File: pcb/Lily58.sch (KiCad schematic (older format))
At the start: 114 parts, among them J1 LED, J2 4PIN, J3 Conn_01x06_Female, P1 i2c_pin, P2 i2c_pin, SW1 SW_PUSH, SW10 SW_PUSH, SW11 SW_PUSH, SW12 SW_PUSH, SW13 SW_PUSH, SW14 SW_PUSH, SW15 SW_PUSH, SW16 SW_PUSH, SW17 SW_PUSH, SW18 SW_PUSH, SW19 SW_PUSH, SW2 SW_PUSH, SW20 SW_PUSH, SW21 SW_PUSH, SW22 SW_PUSH, SW23 SW_PUSH, SW24 SW_PUSH, SW25 SW_PUSH, SW26 SW_PUSH, SW27 SW_PUSH, SW28 SW_PUSH, SW29 SW_PUSH, SW3 SW_PUSH, SW4 SW_PUSH, SW5 SW_PUSH, SW6 SW_PUSH, SW7 SW_PUSH, SW8 SW_PUSH, SW9 SW_PUSH, U1 ProMicro

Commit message: add pinheader and logo
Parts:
- added J4: Conn_01x06_Female, Lily58-footprint:OLED_4Pin, symbol Lily58-rescue:CONN_01X04-Lily58-cache
- added JP10, JP11, JP12, JP13, JP14, JP15, JP16, JP9: Jumper_NO_Small, Lily58-footprint:Jumper, symbol Device:Jumper_NO_Small
- J3: symbol Connector:Conn_01x06_Female -> Lily58-rescue:CONN_01X04-Lily58-cache
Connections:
- net A2: now also JP11.2, JP14.2; no longer J3.6 (Pin_6)
- net A3: now also JP12.2, JP13.2; no longer J3.5 (Pin_5)
- net col0: now also JP10.2, JP15.2
- net row4: now also JP16.2, JP9.2
- new net: J4.1 (P1), JP13.1, JP9.1
- new net: J4.2 (P2), JP10.1, JP14.1
- new net: J4.3 (P3), JP11.1, JP15.1
- new net: J4.4 (P4), JP12.1, JP16.1
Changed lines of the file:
@@
 $EndComp
 $Comp
-L Connector:Conn_01x06_Female J3
+L Lily58-rescue:CONN_01X04-Lily58-cache J3
 U 1 1 6192B632
-P 2550 6250
-F 0 "J3" H 2578 6226 50  0000 L CNN
-F 1 "Conn_01x06_Female" H 2578 6135 50  0000 L CNN
-F 2 "Lily58-footprint:OLED_4Pin" H 2550 6250 50  0001 C CNN
-F 3 "~" H 2550 6250 50  0001 C CNN
-	1    2550 6250
-	1    0    0    -1
+P 2150 6200
+F 0 "J3" H 2178 6176 50  0000 L CNN
+F 1 "Conn_01x06_Female" H 2178 6085 50  0000 L CNN
+F 2 "Lily58-footprint:OLED_4Pin" H 2150 6200 50  0001 C CNN
+F 3 "~" H 2150 6200 50  0001 C CNN
+	1    2150 6200
+	-1   0    0    -1
 $EndComp
 Wire Wire Line
@@
 Text GLabel 4050 2600 2    50   Input ~ 0
 A2
-Text GLabel 2350 6450 0    50   Input ~ 0
-A3
-Text GLabel 2350 6550 0    50   Input ~ 0
-A2
 Text GLabel 5500 7050 0    50   Input ~ 0
 LED
+$Comp
+L Lily58-rescue:CONN_01X04-Lily58-cache J4
+U 1 1 6197A369
+P 2150 7150
+F 0 "J4" H 2178 7126 50  0000 L CNN
+F 1 "Conn_01x06_Female" H 2178 7035 50  0000 L CNN
+F 2 "Lily58-footprint:OLED_4Pin" H 2150 7150 50  0001 C CNN
+F 3 "~" H 2150 7150 50  0001 C CNN
+	1    2150 7150
+	-1   0    0    -1
+$EndComp
+Text GLabel 3050 7300 2    50   Input ~ 0
+A3
+Text GLabel 3050 7200 2    50   Input ~ 0
+A2
+Text GLabel 3050 7100 2    50   Input ~ 0
+col0
+Text GLabel 3050 7000 2    50   Input ~ 0
+row4
+Text GLabel 3050 7500 2    50   Input ~ 0
+A3
+Text GLabel 3050 7600 2    50   Input ~ 0
+A2
+Text GLabel 3050 7700 2    50   Input ~ 0
+col0
+Text GLabel 3050 7800 2    50   Input ~ 0
+row4
+$Comp
+L Device:Jumper_NO_Small JP9
+U 1 1 619CD29F
+P 2950 7000
+F 0 "JP9" H 2950 6950 50  0000 C CNN
+F 1 "Jumper_NO_Small" H 2950 7094 50  0001 C CNN
+F 2 "Lily58-footprint:Jumper" H 2950 7000 50  0001 C CNN
+F 3 "~" H 2950 7000 50  0001 C CNN
+	1    2950 7000
+	1    0    0    -1
+$EndComp
+$Comp
+L Device:Jumper_NO_Small JP10
+U 1 1 619CDE91
+P 2950 7100
+F 0 "JP10" H 2950 7050 50  0000 C CNN
+F 1 "Jumper_NO_Small" H 2950 7194 50  0001 C CNN
+F 2 "Lily58-footprint:Jumper" H 2950 7100 50  0001 C CNN
+F 3 "~" H 2950 7100 50  0001 C CNN
+	1    2950 7100
+	1    0    0    -1
+$EndComp
+$Comp
+L Device:Jumper_NO_Small JP11
+U 1 1 619CDE9B
+P 2950 7200
+F 0 "JP11" H 2950 7150 50  0000 C CNN
+F 1 "Jumper_NO_Small" H 2950 7294 50  0001 C CNN
+F 2 "Lily58-footprint:Jumper" H 2950 7200 50  0001 C CNN
+F 3 "~" H 2950 7200 50  0001 C CNN
+	1    2950 7200
+	1    0    0    -1
+$EndComp
+$Comp
+L Device:Jumper_NO_Small JP12
+U 1 1 619CDEA5
+P 2950 7300
+F 0 "JP12" H 2950 7250 50  0000 C CNN
+F 1 "Jumper_NO_Small" H 2950 7394 50  0001 C CNN
+F 2 "Lily58-footprint:Jumper" H 2950 7300 50  0001 C CNN
+F 3 "~" H 2950 7300 50  0001 C CNN
+	1    2950 7300
+	1    0    0    -1
+$EndComp
+$Comp
+L Device:Jumper_NO_Small JP13
+U 1 1 619CDEAF
+P 2950 7500
+F 0 "JP13" H 2950 7450 50  0000 C CNN
+F 1 "Jumper_NO_Small" H 2950 7594 50  0001 C CNN
+F 2 "Lily58-footprint:Jumper" H 2950 7500 50  0001 C CNN
+F 3 "~" H 2950 7500 50  0001 C CNN
+	1    2950 7500
+	1    0    0    -1
+$EndComp
+$Comp
+L Device:Jumper_NO_Small JP14
+U 1 1 619CDEB9
+P 2950 7600
+F 0 "JP14" H 2950 7550 50  0000 C CNN
+F 1 "Jumper_NO_Small" H 2950 7694 50  0001 C CNN
+F 2 "Lily58-footprint:Jumper" H 2950 7600 50  0001 C CNN
+F 3 "~" H 2950 7600 50  0001 C CNN
+	1    2950 7600
+	1    0    0    -1
+$EndComp
+$Comp
+L Device:Jumper_NO_Small JP15
+U 1 1 619CDEC3
+P 2950 7700
+F 0 "JP15" H 2950 7650 50  0000 C CNN
+F 1 "Jumper_NO_Small" H 2950 7794 50  0001 C CNN
+F 2 "Lily58-footprint:Jumper" H 2950 7700 50  0001 C CNN
+F 3 "~" H 2950 7700 50  0001 C CNN
+	1    2950 7700
+	1    0    0    -1
+$EndComp
+$Comp
+L Device:Jumper_NO_Small JP16
+U 1 1 619CDECD
+P 2950 7800
+F 0 "JP16" H 2950 7750 50  0000 C CNN
+F 1 "Jumper_NO_Small" H 2950 7894 50  0001 C CNN
+F 2 "Lily58-footprint:Jumper" H 2950 7800 50  0001 C CNN
+F 3 "~" H 2950 7800 50  0001 C CNN
+	1    2950 7800
+	1    0    0    -1
+$EndComp
+Wire Wire Line
+	2350 7000 2800 7000
+Wire Wire Line
+	2350 7100 2750 7100
+Wire Wire Line
+	2350 7200 2700 7200
+Wire Wire Line
+	2350 7300 2650 7300
+Wire Wire Line
+	2800 7000 2800 7500
+Wire Wire Line
+	2800 7500 2850 7500
+Connection ~ 2800 7000
+Wire Wire Line
+	2800 7000 2850 7000
+Wire Wire Line
+	2850 7600 2750 7600
+Wire Wire Line
+	2750 7600 2750 7100
+Connection ~ 2750 7100
+Wire Wire Line
+	2750 7100 2850 7100
+Wire Wire Line
+	2850 7700 2700 7700
+Wire Wire Line
+	2700 7700 2700 7200
+Connection ~ 2700 7200
+Wire Wire Line
+	2700 7200 2850 7200
+Wire Wire Line
+	2850 7800 2650 7800
+Wire Wire Line
+	2650 7800 2650 7300
+Connection ~ 2650 7300
+Wire Wire Line
+	2650 7300 2850 7300
 $EndSCHEMATC

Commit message: brush up PCB
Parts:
- removed J1: LED, Lily58-footprint:StripLED, symbol Lily58-rescue:LED-Lily58-cache
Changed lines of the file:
@@
 $EndComp
-$Comp
-L Lily58-rescue:LED-Lily58-cache J1
-U 1 1 5B74AE32
-P 4000 3600
-F 0 "J1" H 4000 3800 50  0000 C CNN
-F 1 "LED" H 4000 3400 50  0000 C CNN
-F 2 "Lily58-footprint:StripLED" H 4000 3600 50  0001 C CNN
-F 3 "" H 4000 3600 50  0001 C CNN
-	1    4000 3600
-	1    0    0    -1
-$EndComp
-$Comp
-L Lily58-rescue:VCC-Lily58-cache #PWR07
-U 1 1 5B74B06A
-P 4200 3500
-F 0 "#PWR07" H 4200 3350 50  0001 C CNN
-F 1 "VCC" H 4217 3673 50  0000 C CNN
-F 2 "" H 4200 3500 50  0001 C CNN
-F 3 "" H 4200 3500 50  0001 C CNN
-	1    4200 3500
-	1    0    0    -1
-$EndComp
-$Comp
-L Lily58-rescue:GND-Lily58-cache #PWR08
-U 1 1 5B74B15A
-P 4200 3700
-F 0 "#PWR08" H 4200 3450 50  0001 C CNN
-F 1 "GND" H 4205 3527 50  0000 C CNN
-F 2 "" H 4200 3700 50  0001 C CNN
-F 3 "" H 4200 3700 50  0001 C CNN
-	1    4200 3700
-	1    0    0    -1
-$EndComp
-Text GLabel 4200 3600 2    50   Input ~ 0
-LED
 $Comp
 L Lily58-rescue:GND-Lily58-cache #PWR010

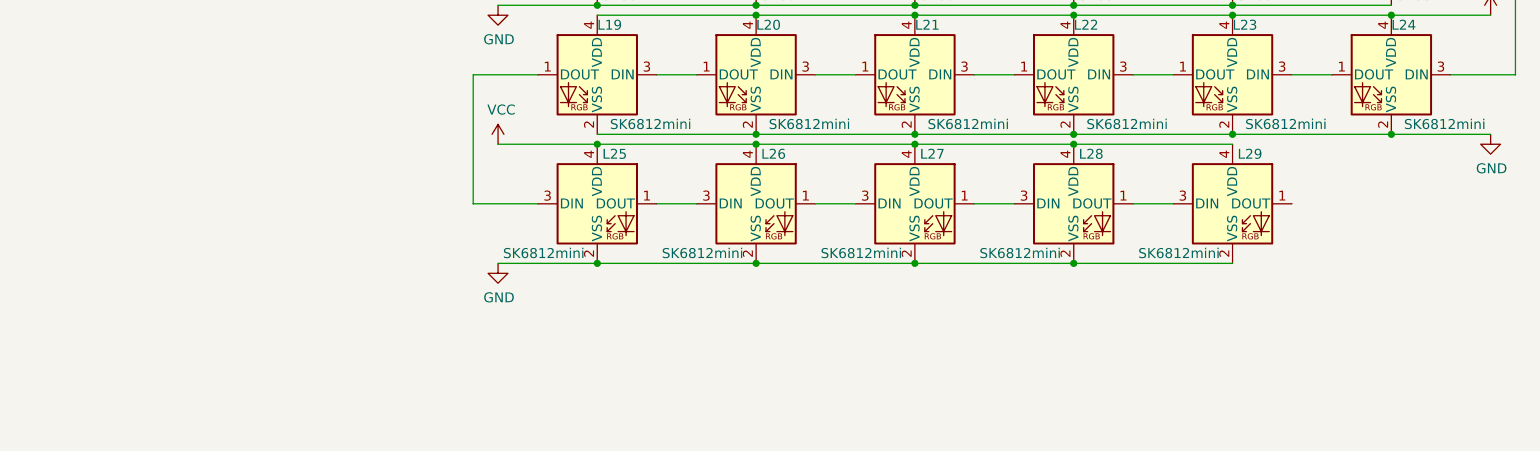
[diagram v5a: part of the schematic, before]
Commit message: add sk6812mini
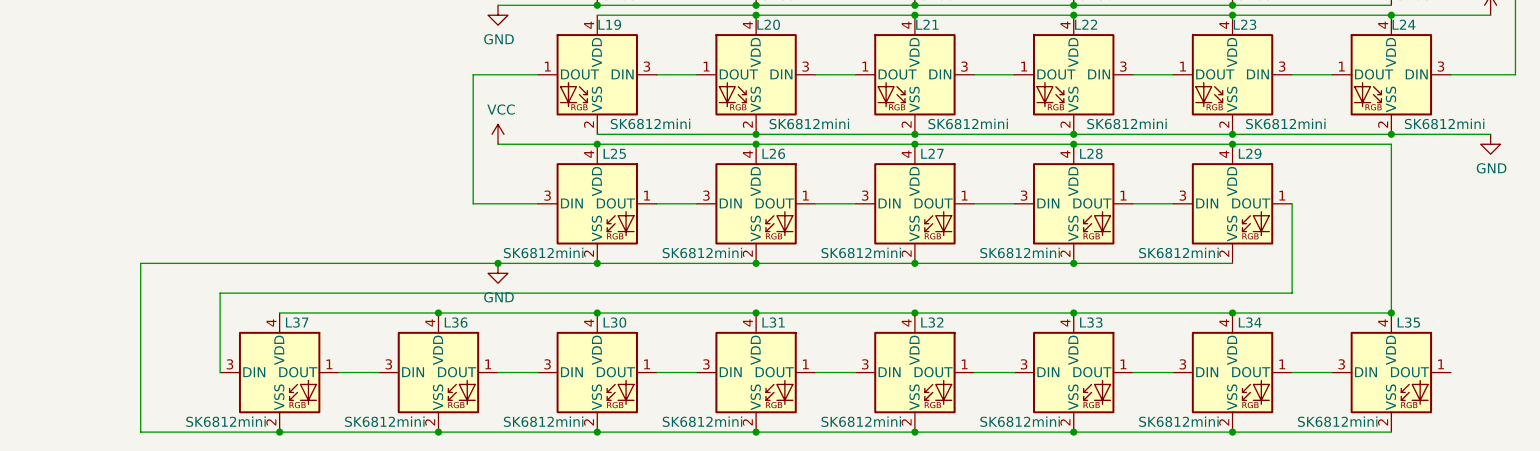
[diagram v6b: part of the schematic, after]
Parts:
- added L30, L31, L32, L33, L34, L35, L36, L37: SK6812mini, Lily58-footprint:SK6812MINI_underglow_rev, symbol LED:SK6812MINI
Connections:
- net GND: now also L30.2 (VSS), L31.2 (VSS), L32.2 (VSS), L33.2 (VSS), L34.2 (VSS), L35.2 (VSS), L36.2 (VSS), L37.2 (VSS)
- net VCC: now also L30.4 (VDD), L31.4 (VDD), L32.4 (VDD), L33.4 (VDD), L34.4 (VDD), L35.4 (VDD), L36.4 (VDD), L37.4 (VDD)
- net at L29.1 (DOUT): now also L37.3 (DIN)
- new net: L33.1 (DOUT), L34.3 (DIN)
- new net: L32.1 (DOUT), L33.3 (DIN)
- new net: L31.1 (DOUT), L32.3 (DIN)
- new net: L30.1 (DOUT), L31.3 (DIN)
- new net: L30.3 (DIN), L36.1 (DOUT)
- new net: L34.1 (DOUT), L35.3 (DIN)
- new net: L36.3 (DIN), L37.1 (DOUT)
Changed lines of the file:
@@
 	5500 7700 5175 7700
 Connection ~ 5800 9950
-Wire Wire Line
-	5300 9950 5800 9950
 Connection ~ 5800 8650
 Wire Wire Line
@@
 Wire Wire Line
 	2650 7300 2850 7300
+Wire Wire Line
+	7700 10500 7900 10500
+Wire Wire Line
+	6900 10500 7100 10500
+$Comp
+L LED:SK6812MINI L33
+U 1 1 61A4CA14
+P 8200 10500
+F 0 "L33" H 8225 10750 50  0000 L CNN
+F 1 "SK6812mini" H 7725 10250 50  0000 L CNN
+F 2 "Lily58-footprint:SK6812MINI_underglow_rev" H 8250 10200 50  0001 L TNN
+F 3 "https://cdn-shop.adafruit.com/product-files/2686/SK6812MINI_REV.01-1-2.pdf" H 8300 10125 50  0001 L TNN
+	1    8200 10500
+	1    0    0    -1
+$EndComp
+$Comp
+L LED:SK6812MINI L32
+U 1 1 61A4CA1E
+P 7400 10500
+F 0 "L32" H 7425 10750 50  0000 L CNN
+F 1 "SK6812mini" H 6925 10250 50  0000 L CNN
+F 2 "Lily58-footprint:SK6812MINI_underglow_rev" H 7450 10200 50  0001 L TNN
+F 3 "https://cdn-shop.adafruit.com/product-files/2686/SK6812MINI_REV.01-1-2.pdf" H 7500 10125 50  0001 L TNN
+	1    7400 10500
+	1    0    0    -1
+$EndComp
+Wire Wire Line
+	6100 10500 6300 10500
+$Comp
+L LED:SK6812MINI L31
+U 1 1 61A4CA29
+P 6600 10500
+F 0 "L31" H 6625 10750 50  0000 L CNN
+F 1 "SK6812mini" H 6125 10250 50  0000 L CNN
+F 2 "Lily58-footprint:SK6812MINI_underglow_rev" H 6650 10200 50  0001 L TNN
+F 3 "https://cdn-shop.adafruit.com/product-files/2686/SK6812MINI_REV.01-1-2.pdf" H 6700 10125 50  0001 L TNN
+	1    6600 10500
+	1    0    0    -1
+$EndComp
+$Comp
+L LED:SK6812MINI L30
+U 1 1 61A4CA33
+P 5800 10500
+F 0 "L30" H 5825 10750 50  0000 L CNN
+F 1 "SK6812mini" H 5325 10250 50  0000 L CNN
+F 2 "Lily58-footprint:SK6812MINI_underglow_rev" H 5850 10200 50  0001 L TNN
+F 3 "https://cdn-shop.adafruit.com/product-files/2686/SK6812MINI_REV.01-1-2.pdf" H 5900 10125 50  0001 L TNN
+	1    5800 10500
+	1    0    0    -1
+$EndComp
+$Comp
+L LED:SK6812MINI L34
+U 1 1 61A4CA3D
+P 9000 10500
+F 0 "L34" H 9025 10750 50  0000 L CNN
+F 1 "SK6812mini" H 8525 10250 50  0000 L CNN
+F 2 "Lily58-footprint:SK6812MINI_underglow_rev" H 9050 10200 50  0001 L TNN
+F 3 "https://cdn-shop.adafruit.com/product-files/2686/SK6812MINI_REV.01-1-2.pdf" H 9100 10125 50  0001 L TNN
+	1    9000 10500
+	1    0    0    -1
+$EndComp
+Wire Wire Line
+	8500 10500 8700 10500
+$Comp
+L LED:SK6812MINI L35
+U 1 1 61A7E919
+P 9800 10500
+F 0 "L35" H 9825 10750 50  0000 L CNN
+F 1 "SK6812mini" H 9325 10250 50  0000 L CNN
+F 2 "Lily58-footprint:SK6812MINI_underglow_rev" H 9850 10200 50  0001 L TNN
+F 3 "https://cdn-shop.adafruit.com/product-files/2686/SK6812MINI_REV.01-1-2.pdf" H 9900 10125 50  0001 L TNN
+	1    9800 10500
+	1    0    0    -1
+$EndComp
+Wire Wire Line
+	9300 10500 9500 10500
+Wire Wire Line
+	5800 10200 6600 10200
+Connection ~ 6600 10200
+Wire Wire Line
+	6600 10200 7400 10200
+Connection ~ 7400 10200
+Wire Wire Line
+	7400 10200 8200 10200
+Connection ~ 8200 10200
+Wire Wire Line
+	8200 10200 9000 10200
+Connection ~ 9000 10200
+Wire Wire Line
+	9000 10200 9800 10200
+Wire Wire Line
+	9000 9350 9800 9350
+Connection ~ 9000 9350
+Connection ~ 9800 10200
+Wire Wire Line
+	9800 10800 9000 10800
+Connection ~ 5800 10800
+Connection ~ 6600 10800
+Wire Wire Line
+	6600 10800 5800 10800
+Connection ~ 7400 10800
+Wire Wire Line
+	7400 10800 6600 10800
+Connection ~ 8200 10800
+Wire Wire Line
+	8200 10800 7400 10800
+Connection ~ 9000 10800
+Wire Wire Line
+	9000 10800 8200 10800
+Wire Wire Line
+	5300 9950 5800 9950
+$Comp
+L LED:SK6812MINI L36
+U 1 1 61AA0F7C
+P 5000 10500
+F 0 "L36" H 5025 10750 50  0000 L CNN
+F 1 "SK6812mini" H 4525 10250 50  0000 L CNN
+F 2 "Lily58-footprint:SK6812MINI_underglow_rev" H 5050 10200 50  0001 L TNN
+F 3 "https://cdn-shop.adafruit.com/product-files/2686/SK6812MINI_REV.01-1-2.pdf" H 5100 10125 50  0001 L TNN
+	1    5000 10500
+	1    0    0    -1
+$EndComp
+Wire Wire Line
+	5300 10500 5500 10500
+Wire Wire Line
+	5000 10800 5800 10800
+Wire Wire Line
+	5000 10200 5800 10200
+Connection ~ 5800 10200
+Connection ~ 5000 10800
+Connection ~ 5300 9950
+Wire Wire Line
+	9800 9350 9800 10200
+Wire Wire Line
+	9300 9650 9300 10100
+$Comp
+L LED:SK6812MINI L37
+U 1 1 61A982D1
+P 4200 10500
+F 0 "L37" H 4225 10750 50  0000 L CNN
+F 1 "SK6812mini" H 3725 10250 50  0000 L CNN
+F 2 "Lily58-footprint:SK6812MINI_underglow_rev" H 4250 10200 50  0001 L TNN
+F 3 "https://cdn-shop.adafruit.com/product-files/2686/SK6812MINI_REV.01-1-2.pdf" H 4300 10125 50  0001 L TNN
+	1    4200 10500
+	1    0    0    -1
+$EndComp
+Wire Wire Line
+	4200 10800 5000 10800
+Wire Wire Line
+	4200 10800 3500 10800
+Wire Wire Line
+	3500 10800 3500 9950
+Wire Wire Line
+	3500 9950 5300 9950
+Connection ~ 4200 10800
+Wire Wire Line
+	3900 10100 3900 10500
+Wire Wire Line
+	3900 10100 9300 10100
+Wire Wire Line
+	4500 10500 4700 10500
+Wire Wire Line
+	4200 10200 5000 10200
+Connection ~ 5000 10200
 $EndSCHEMATC
